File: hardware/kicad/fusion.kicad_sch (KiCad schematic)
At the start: 32 parts, among them J1 BATTERY, J2 LSM6DSOX, J3 PICKIT, J4 HC-05, J5 FLEX, J7 FTDI, SW1 BUTTON, SW2 POWER, SW3 UART, U1 MCP1603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

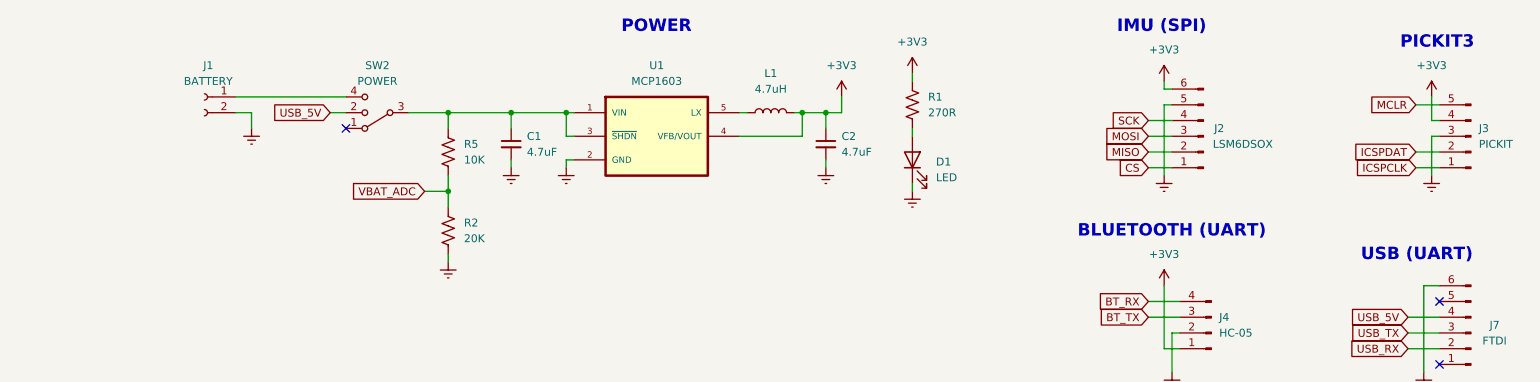
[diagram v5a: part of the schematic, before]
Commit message: Power HC-05 from raw power source
BT module has an LDO that requires at least 3V6.
Powering from 3V3 causes improper regulation and
browns out the entire system.
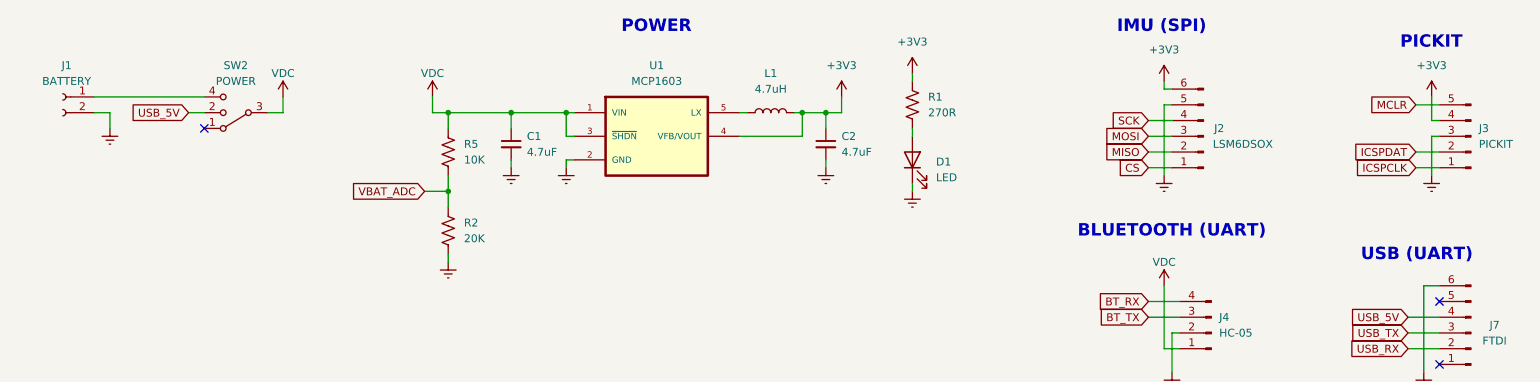
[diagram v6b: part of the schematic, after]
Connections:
- net +3V3: no longer J4.1 (Pin_1)
- net VDC: now reaches C1.1, R5.1, SW2.3, U1.1 (VIN), U1.3 (~{SHDN})
- net VDC: now also J4.1 (Pin_1)
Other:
- note added: "PICKIT"
- note removed: "PICKIT3"
- moved on the sheet: J1, SW2
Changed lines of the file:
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@@
   (junction (at 35.56 114.3) (diameter 0) (color 0 0 0 0)
   )
+  (junction (at 26.67 171.45) (diameter 0) (color 0 0 0 0)
+  )
   (junction (at 93.98 38.1) (diameter 0) (color 0 0 0 0)
   )
-  (junction (at 26.67 171.45) (diameter 0) (color 0 0 0 0)
-  )
   (junction (at 90.17 171.45) (diameter 0) (color 0 0 0 0)
   )
@@
   (junction (at 49.53 161.29) (diameter 0) (color 0 0 0 0)
   )
-  (no_connect (at 77.47 40.64))
+  (no_connect (at 54.61 40.64))
   (no_connect (at 254 68.58))
   (no_connect (at 254 78.74))
@@
     (stroke (width 0) (type default) (color 0 0 0 0))
   )
-  (wire (pts (xy 87.63 38.1) (xy 93.98 38.1))
-    (stroke (width 0) (type default) (color 0 0 0 0))
-  )
   (wire (pts (xy 26.67 171.45) (xy 26.67 173.99))
     (stroke (width 0) (type default) (color 0 0 0 0))
@@
     (stroke (width 0) (type default) (color 0 0 0 0))
   )
+  (wire (pts (xy 91.44 38.1) (xy 93.98 38.1))
+    (stroke (width 0) (type default) (color 0 0 0 0))
+  )
   (wire (pts (xy 35.56 118.11) (xy 35.56 114.3))
     (stroke (width 0) (type default) (color 0 0 0 0))
@@
     (stroke (width 0) (type default) (color 0 0 0 0))
   )
+  (wire (pts (xy 91.44 35.56) (xy 91.44 38.1))
+    (stroke (width 0) (type default) (color 0 0 0 0))
+  )
   (wire (pts (xy 80.01 151.13) (xy 80.01 152.4))
     (stroke (width 0) (type default) (color 0 0 0 0))
@@
     (stroke (width 0) (type default) (color 0 0 0 0))
   )
-  (wire (pts (xy 62.23 40.64) (xy 62.23 38.1))
+  (wire (pts (xy 39.37 40.64) (xy 39.37 38.1))
     (stroke (width 0) (type default) (color 0 0 0 0))
   )
@@
     (stroke (width 0) (type default) (color 0 0 0 0))
   )
-  (wire (pts (xy 59.69 38.1) (xy 62.23 38.1))
+  (wire (pts (xy 36.83 38.1) (xy 39.37 38.1))
     (stroke (width 0) (type default) (color 0 0 0 0))
   )
@@
     (stroke (width 0) (type default) (color 0 0 0 0))
   )
-  (wire (pts (xy 74.93 38.1) (xy 77.47 38.1))
+  (wire (pts (xy 52.07 38.1) (xy 54.61 38.1))
+    (stroke (width 0) (type default) (color 0 0 0 0))
+  )
+  (wire (pts (xy 67.31 35.56) (xy 67.31 38.1))
     (stroke (width 0) (type default) (color 0 0 0 0))
   )
@@
     (stroke (width 0) (type default) (color 0 0 0 0))
   )
-  (wire (pts (xy 59.69 35.56) (xy 77.47 35.56))
+  (wire (pts (xy 36.83 35.56) (xy 54.61 35.56))
     (stroke (width 0) (type default) (color 0 0 0 0))
   )
@@
   )
   (wire (pts (xy 151.13 41.91) (xy 151.13 38.1))
+    (stroke (width 0) (type default) (color 0 0 0 0))
+  )
+  (wire (pts (xy 64.77 38.1) (xy 67.31 38.1))
     (stroke (width 0) (type default) (color 0 0 0 0))
   )
@@
     (effects (font (size 2 2) (thickness 0.254) bold) (justify left bottom))
   )
-  (text "PICKIT3" (at 247.65 27.94 0)
+  (text "PICKIT" (at 247.65 27.94 0)
     (effects (font (size 2 2) (thickness 0.254) bold) (justify left bottom))
   )
@@
     )
   )
-  (global_label "USB_5V" (shape input) (at 74.93 38.1 180) (fields_autoplaced)
-    (effects (font (size 1.27 1.27)) (justify right))
-    (property "Intersheet References" "${INTERSHEET_REFS}" (id 0) (at 65.4412 38.0206 0)
+  (global_label "USB_5V" (shape input) (at 52.07 38.1 180) (fields_autoplaced)
+    (effects (font (size 1.27 1.27)) (justify right))
+    (property "Intersheet References" "${INTERSHEET_REFS}" (id 0) (at 42.5812 38.0206 0)
       (effects (font (size 1.27 1.27)) (justify right) hide)
     )
@@
     (pin "5")
   )
+  (symbol (lib_id "power:VDC") (at 209.55 66.04 0) (unit 1)
+    (in_bom yes) (on_board yes)
+    (property "Reference" "#PWR0110" (id 0) (at 209.55 68.58 0)
+      (effects (font (size 1.27 1.27)) hide)
+    )
+    (property "Value" "VDC" (id 1) (at 209.55 62.23 0))
+    (property "Footprint" "" (id 2) (at 209.55 66.04 0)
+      (effects (font (size 1.27 1.27)) hide)
+    )
+    (property "Datasheet" "" (id 3) (at 209.55 66.04 0)
+      (effects (font (size 1.27 1.27)) hide)
+    )
+    (pin "1")
+  )
   (symbol (lib_id "Device:LED") (at 168.91 45.72 90) (unit 1)
     (in_bom yes) (on_board yes) (fields_autoplaced)
@@
     )
     (property "Datasheet" "" (id 3) (at 59.69 180.34 0)
+      (effects (font (size 1.27 1.27)) hide)
+    )
+    (pin "1")
+  )
+  (symbol (lib_id "power:VDC") (at 67.31 35.56 0) (unit 1)
+    (in_bom yes) (on_board yes)
+    (property "Reference" "#PWR0109" (id 0) (at 67.31 38.1 0)
+      (effects (font (size 1.27 1.27)) hide)
+    )
+    (property "Value" "VDC" (id 1) (at 67.31 31.75 0))
+    (property "Footprint" "" (id 2) (at 67.31 35.56 0)
+      (effects (font (size 1.27 1.27)) hide)
+    )
+    (property "Datasheet" "" (id 3) (at 67.31 35.56 0)
       (effects (font (size 1.27 1.27)) hide)
     )
@@
     (pin "3")
   )
-  (symbol (lib_id "Connector:Conn_01x02_Female") (at 54.61 35.56 0) (mirror y) (unit 1)
-    (in_bom yes) (on_board yes) (fields_autoplaced)
-    (property "Reference" "J1" (id 0) (at 55.245 30.48 0))
-    (property "Value" "BATTERY" (id 1) (at 55.245 33.02 0))
-    (property "Footprint" "Fusion:JST" (id 2) (at 54.61 35.56 0)
-      (effects (font (size 1.27 1.27)) hide)
-    )
-    (property "Datasheet" "~" (id 3) (at 54.61 35.56 0)
+  (symbol (lib_id "Connector:Conn_01x02_Female") (at 31.75 35.56 0) (mirror y) (unit 1)
+    (in_bom yes) (on_board yes) (fields_autoplaced)
+    (property "Reference" "J1" (id 0) (at 32.385 30.48 0))
+    (property "Value" "BATTERY" (id 1) (at 32.385 33.02 0))
+    (property "Footprint" "Fusion:JST" (id 2) (at 31.75 35.56 0)
+      (effects (font (size 1.27 1.27)) hide)
+    )
+    (property "Datasheet" "~" (id 3) (at 31.75 35.56 0)
       (effects (font (size 1.27 1.27)) hide)
     )
@@
     (pin "4")
   )
-  (symbol (lib_id "power:GNDREF") (at 62.23 40.64 0) (unit 1)
-    (in_bom yes) (on_board yes) (fields_autoplaced)
-    (property "Reference" "#PWR0104" (id 0) (at 62.23 46.99 0)
-      (effects (font (size 1.27 1.27)) hide)
-    )
-    (property "Value" "GNDREF" (id 1) (at 62.23 45.72 0)
-      (effects (font (size 1.27 1.27)) hide)
-    )
-    (property "Footprint" "" (id 2) (at 62.23 40.64 0)
-      (effects (font (size 1.27 1.27)) hide)
-    )
-    (property "Datasheet" "" (id 3) (at 62.23 40.64 0)
+  (symbol (lib_id "power:GNDREF") (at 39.37 40.64 0) (unit 1)
+    (in_bom yes) (on_board yes) (fields_autoplaced)
+    (property "Reference" "#PWR0104" (id 0) (at 39.37 46.99 0)
+      (effects (font (size 1.27 1.27)) hide)
+    )
+    (property "Value" "GNDREF" (id 1) (at 39.37 45.72 0)
+      (effects (font (size 1.27 1.27)) hide)
+    )
+    (property "Footprint" "" (id 2) (at 39.37 40.64 0)
+      (effects (font (size 1.27 1.27)) hide)
+    )
+    (property "Datasheet" "" (id 3) (at 39.37 40.64 0)
       (effects (font (size 1.27 1.27)) hide)
     )
@@
     (pin "1")
   )
+  (symbol (lib_id "power:VDC") (at 91.44 35.56 0) (unit 1)
+    (in_bom yes) (on_board yes)
+    (property "Reference" "#PWR0108" (id 0) (at 91.44 38.1 0)
+      (effects (font (size 1.27 1.27)) hide)
+    )
+    (property "Value" "VDC" (id 1) (at 91.44 31.75 0))
+    (property "Footprint" "" (id 2) (at 91.44 35.56 0)
+      (effects (font (size 1.27 1.27)) hide)
+    )
+    (property "Datasheet" "" (id 3) (at 91.44 35.56 0)
+      (effects (font (size 1.27 1.27)) hide)
+    )
+    (pin "1")
+  )
   (symbol (lib_id "power:GNDREF") (at 49.53 180.34 0) (unit 1)
     (in_bom yes) (on_board yes) (fields_autoplaced)
@@
     )
     (property "Datasheet" "" (id 3) (at 26.67 173.99 0)
-      (effects (font (size 1.27 1.27)) hide)
-    )
-    (pin "1")
-  )
-  (symbol (lib_id "power:+3V3") (at 209.55 66.04 0) (unit 1)
-    (in_bom yes) (on_board yes) (fields_autoplaced)
-    (property "Reference" "#PWR010" (id 0) (at 209.55 69.85 0)
-      (effects (font (size 1.27 1.27)) hide)
-    )
-    (property "Value" "+3V3" (id 1) (at 209.55 60.96 0))
-    (property "Footprint" "" (id 2) (at 209.55 66.04 0)
-      (effects (font (size 1.27 1.27)) hide)
-    )
-    (property "Datasheet" "" (id 3) (at 209.55 66.04 0)
       (effects (font (size 1.27 1.27)) hide)
     )
@@
     (pin "2")
   )
-  (symbol (lib_id "Switch:SW_SP3T") (at 82.55 38.1 180) (unit 1)
-    (in_bom yes) (on_board yes) (fields_autoplaced)
-    (property "Reference" "SW2" (id 0) (at 82.55 30.48 0))
-    (property "Value" "POWER" (id 1) (at 82.55 33.02 0))
-    (property "Footprint" "Fusion:SP3T" (id 2) (at 98.425 42.545 0)
-      (effects (font (size 1.27 1.27)) hide)
-    )
-    (property "Datasheet" "~" (id 3) (at 98.425 42.545 0)
+  (symbol (lib_id "Switch:SW_SP3T") (at 59.69 38.1 180) (unit 1)
+    (in_bom yes) (on_board yes) (fields_autoplaced)
+    (property "Reference" "SW2" (id 0) (at 59.69 30.48 0))
+    (property "Value" "POWER" (id 1) (at 59.69 33.02 0))
+    (property "Footprint" "Fusion:SP3T" (id 2) (at 75.565 42.545 0)
+      (effects (font (size 1.27 1.27)) hide)
+    )
+    (property "Datasheet" "~" (id 3) (at 75.565 42.545 0)
       (effects (font (size 1.27 1.27)) hide)
     )
@@
       (reference "#PWR09") (unit 1) (value "GNDREF") (footprint "")
     )
-    (path "/b20c810a-6938-48c8-9ed6-0b4d45a6c4f9"
-      (reference "#PWR010") (unit 1) (value "+3V3") (footprint "")
-    )
     (path "/62466843-59bf-4608-a085-f36cbc5df554"
       (reference "#PWR011") (unit 1) (value "GNDREF") (footprint "")
@@
       (reference "#PWR0107") (unit 1) (value "+3V3") (footprint "")
     )
+    (path "/a59991ef-dde8-4260-8443-99f465aa7ed6"
+      (reference "#PWR0108") (unit 1) (value "VDC") (footprint "")
+    )
+    (path "/33fb9765-5606-4ff4-b8a5-572b3e45806f"
+      (reference "#PWR0109") (unit 1) (value "VDC") (footprint "")
+    )
+    (path "/1ac68fc2-7c64-4573-ab61-063cd62c1783"
+      (reference "#PWR0110") (unit 1) (value "VDC") (footprint "")
+    )
     (path "/7e5f6eaa-158a-4008-9e69-c821698a53f5"

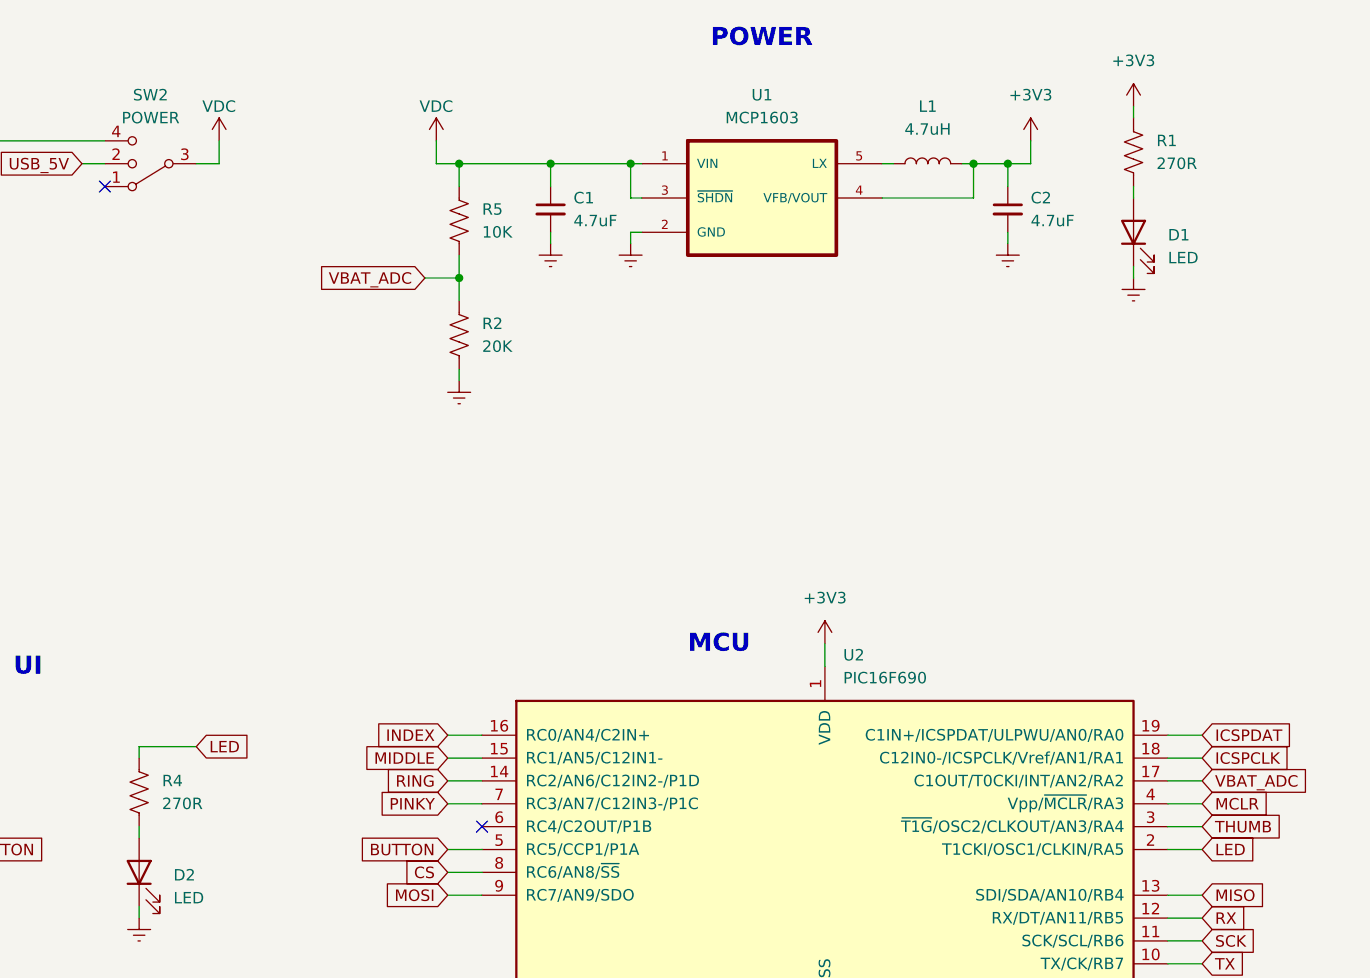
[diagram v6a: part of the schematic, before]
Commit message: Change LED resistors to 200R (DigiKey availability)
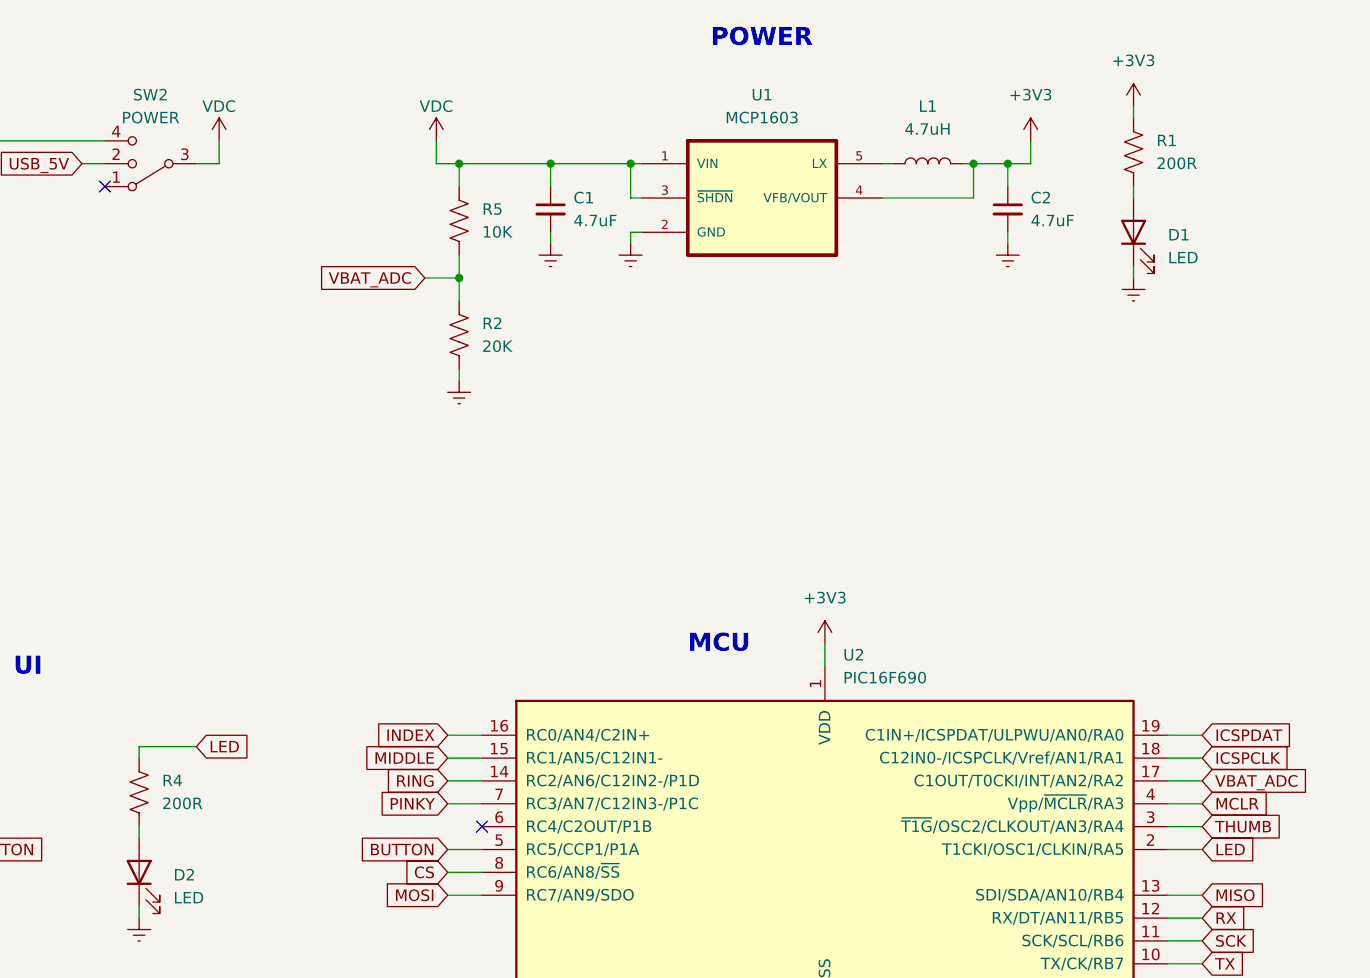
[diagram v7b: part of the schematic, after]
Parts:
- R1, R4: value 270R -> 200R
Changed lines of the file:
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@@
       (effects (font (size 1.27 1.27)) (justify right))
     )
-    (property "Value" "270R" (id 1) (at 171.45 38.0999 0)
+    (property "Value" "200R" (id 1) (at 171.45 38.0999 0)
       (effects (font (size 1.27 1.27)) (justify right))
     )
@@
       (effects (font (size 1.27 1.27)) (justify right))
     )
-    (property "Value" "270R" (id 1) (at 60.96 109.2199 0)
+    (property "Value" "200R" (id 1) (at 60.96 109.2199 0)
       (effects (font (size 1.27 1.27)) (justify right))
     )
@@
     )
     (path "/aa11bcd6-4a41-4882-8d8b-423f845f7cd1"
-      (reference "R1") (unit 1) (value "270R") (footprint "Resistor_SMD:R_0603_1608Metric_Pad0.98x0.95mm_HandSolder")
+      (reference "R1") (unit 1) (value "200R") (footprint "Resistor_SMD:R_0603_1608Metric_Pad0.98x0.95mm_HandSolder")
     )
     (path "/1f601946-0139-4682-8421-7cd20232376e"
@@
     )
     (path "/fdd90794-8a70-4f1e-8ba2-a31b07d0ddc1"
-      (reference "R4") (unit 1) (value "270R") (footprint "Resistor_SMD:R_0603_1608Metric_Pad0.98x0.95mm_HandSolder")
+      (reference "R4") (unit 1) (value "200R") (footprint "Resistor_SMD:R_0603_1608Metric_Pad0.98x0.95mm_HandSolder")
     )
     (path "/7fc32e22-3110-4b46-8606-afcca554e179"
